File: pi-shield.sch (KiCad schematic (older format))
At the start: 46 parts, among them J1 Conn_02x20_Odd_Even, J10 Conn_01x04, J11 a, J12 Conn_01x03, J2 Conn_01x04, J3 Conn_01x04, J4 0530470210, J5 Conn_01x05, J6 Conn_01x07, J7 0530471410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

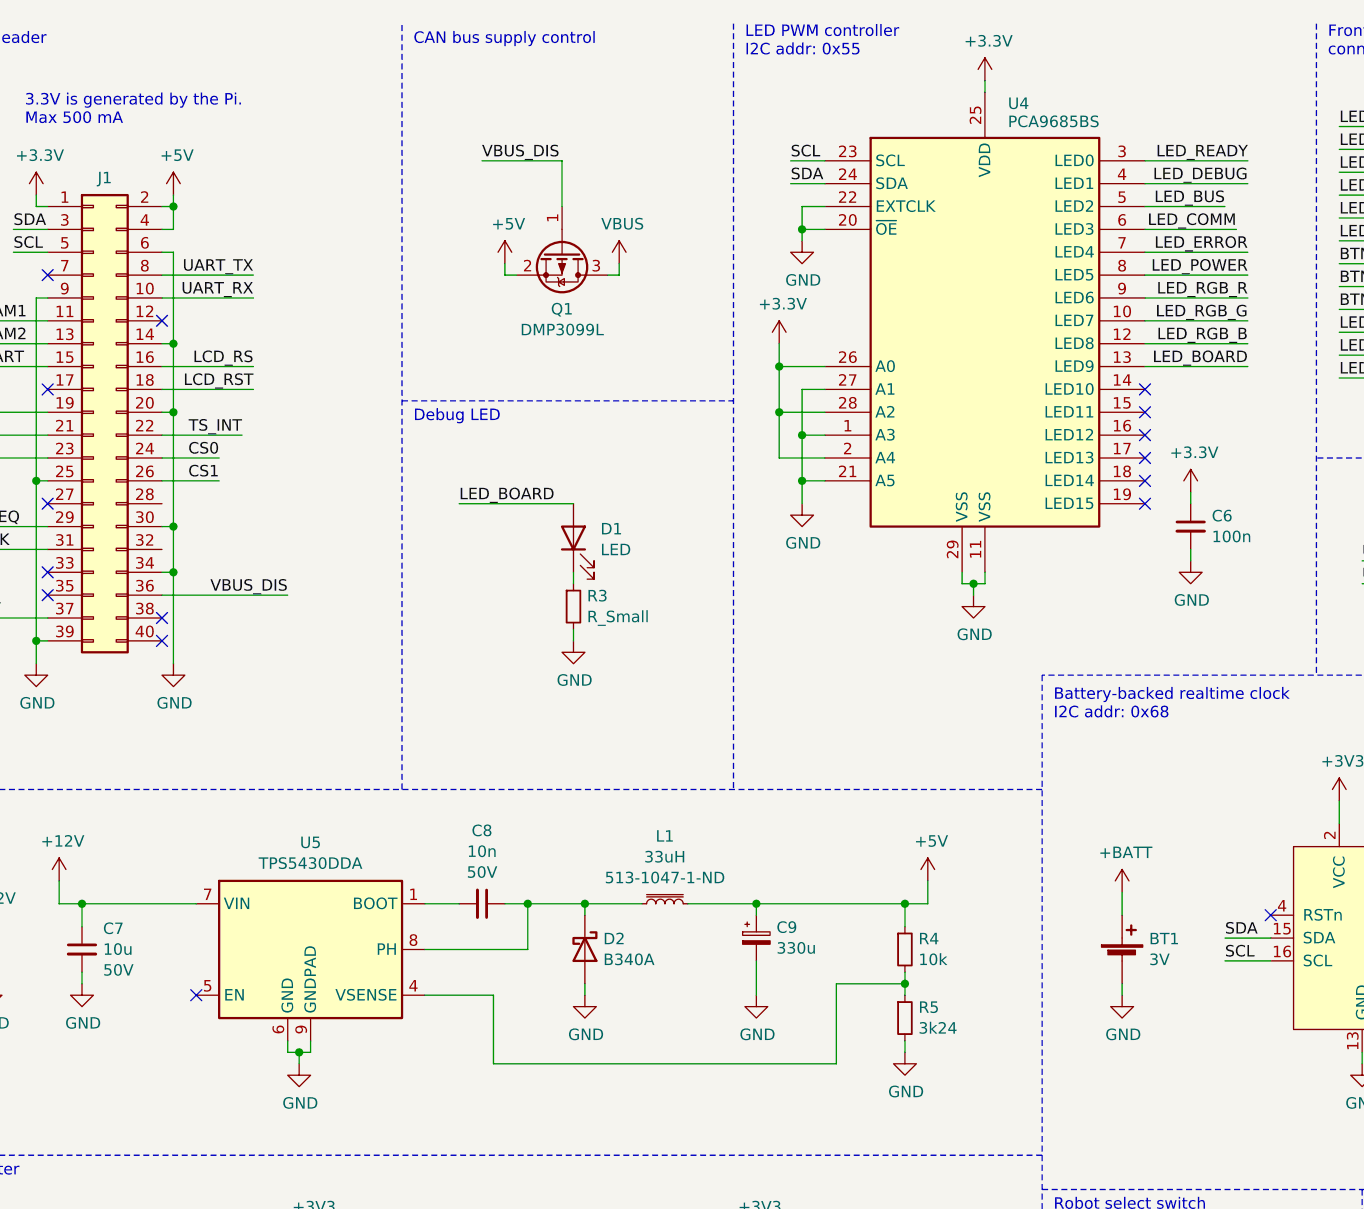
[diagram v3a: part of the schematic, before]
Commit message: Initial component placement
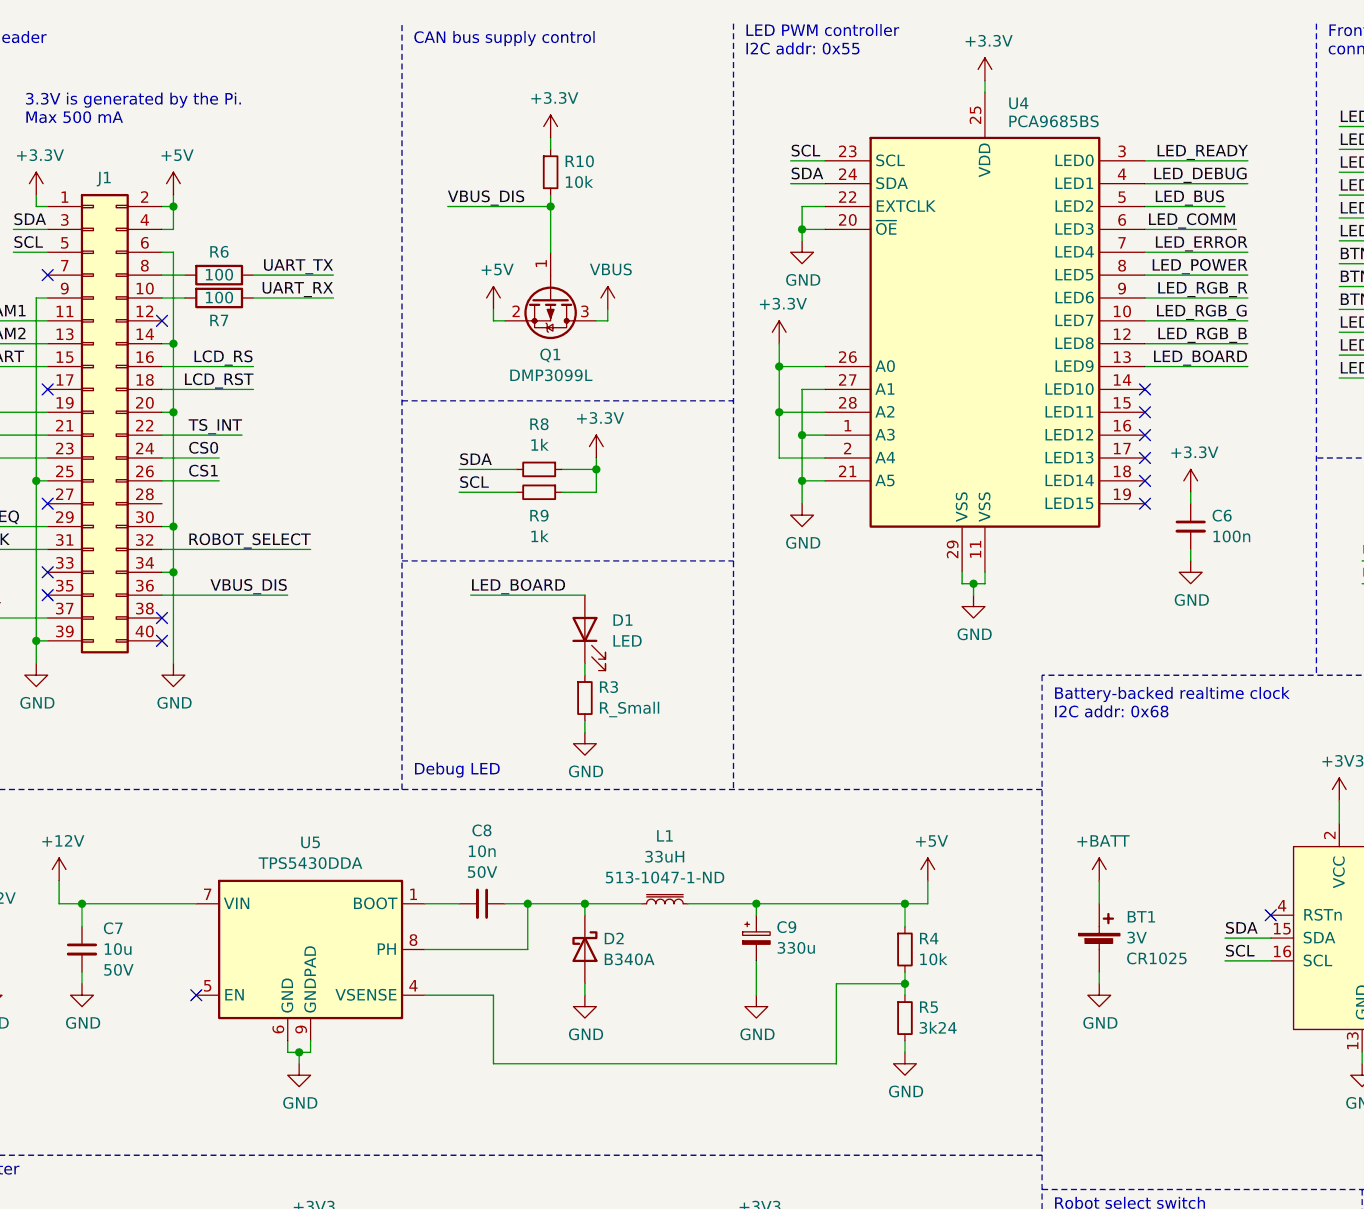
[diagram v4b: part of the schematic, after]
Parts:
- added R10: 10k, Resistor_SMD:R_0603_1608Metric, symbol Device:R_Small
- added R6, R7: 100, Resistor_SMD:R_0603_1608Metric, symbol Device:R
- added R8, R9: 1k, Resistor_SMD:R_0603_1608Metric, symbol Device:R_Small
- BT1: footprint (none) -> pi-shield:3030; battery (none) -> CR1025; digikey# (none) -> 36-3030-ND
- J10: footprint Connector_Molex:Molex_PicoBlade_53048-0410_1x04_P1.25mm_Horizontal -> Connector_Molex:Molex_PicoBlade_53261-0471_1x04-1MP_P1.25mm_Horizontal
- J11: value a -> 0530470210; footprint (none) -> Connector_Molex:Molex_PicoBlade_53398-0271_1x02-1MP_P1.25mm_Vertical
- J2, J3: footprint Connector_Molex:Molex_PicoBlade_53047-0410_1x04_P1.25mm_Vertical -> Connector_Molex:Molex_PicoBlade_53398-0471_1x04-1MP_P1.25mm_Vertical
- L1: footprint (none) -> pi-shield:DR127
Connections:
- net +3V3: now also R10.1, R8.1, R9.1
- net ROBOT_SELECT: now also J1.32 (Pin_32)
- net SCL: now also R9.2
- net SDA: now also R8.2
- net UART_RX: now also R7.1; no longer J1.10 (Pin_10)
- net UART_TX: now also R6.1; no longer J1.8 (Pin_8)
- net VBUS_DIS: now also R10.2
- new net: J1.10 (Pin_10), R7.2
- new net: J1.8 (Pin_8), R6.2
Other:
- moved on the sheet: BT1, D1, Q1, R3

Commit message: Made some progress with layout
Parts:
- R1, R2, R3: footprint Resistor_SMD:R_0805_2012Metric_Pad1.15x1.40mm_HandSolder -> Resistor_SMD:R_0603_1608Metric
- R4, R5: footprint Resistor_SMD:R_0805_2012Metric -> Resistor_SMD:R_0603_1608Metric
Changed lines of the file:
@@
 F 0 "R1" V 3004 7300 50  0000 C CNN
 F 1 "10k" V 3095 7300 50  0000 C CNN
-F 2 "Resistor_SMD:R_0805_2012Metric_Pad1.15x1.40mm_HandSolder" H 3200 7300 50  0001 C CNN
+F 2 "Resistor_SMD:R_0603_1608Metric" H 3200 7300 50  0001 C CNN
 F 3 "~" H 3200 7300 50  0001 C CNN
 	1    3200 7300
@@
 F 0 "R2" H 6591 6346 50  0000 R CNN
 F 1 "10k" H 6591 6255 50  0000 R CNN
-F 2 "Resistor_SMD:R_0805_2012Metric_Pad1.15x1.40mm_HandSolder" H 6650 6300 50  0001 C CNN
+F 2 "Resistor_SMD:R_0603_1608Metric" H 6650 6300 50  0001 C CNN
 F 3 "~" H 6650 6300 50  0001 C CNN
 	1    6650 6300
@@
 F 0 "R3" H 3659 3496 50  0000 L CNN
 F 1 "R_Small" H 3659 3405 50  0000 L CNN
-F 2 "Resistor_SMD:R_0805_2012Metric_Pad1.15x1.40mm_HandSolder" H 3600 3450 50  0001 C CNN
+F 2 "Resistor_SMD:R_0603_1608Metric" H 3600 3450 50  0001 C CNN
 F 3 "~" H 3600 3450 50  0001 C CNN
 	1    3600 3450
@@
 F 0 "R5" H 5059 4896 50  0000 L CNN
 F 1 "3k24" H 5059 4805 50  0000 L CNN
-F 2 "Resistor_SMD:R_0805_2012Metric" H 5000 4850 50  0001 C CNN
+F 2 "Resistor_SMD:R_0603_1608Metric" H 5000 4850 50  0001 C CNN
 F 3 "~" H 5000 4850 50  0001 C CNN
 	1    5000 4850
@@
 F 0 "R4" H 5059 4596 50  0000 L CNN
 F 1 "10k" H 5059 4505 50  0000 L CNN
-F 2 "Resistor_SMD:R_0805_2012Metric" H 5000 4550 50  0001 C CNN
+F 2 "Resistor_SMD:R_0603_1608Metric" H 5000 4550 50  0001 C CNN
 F 3 "~" H 5000 4550 50  0001 C CNN
 	1    5000 4550

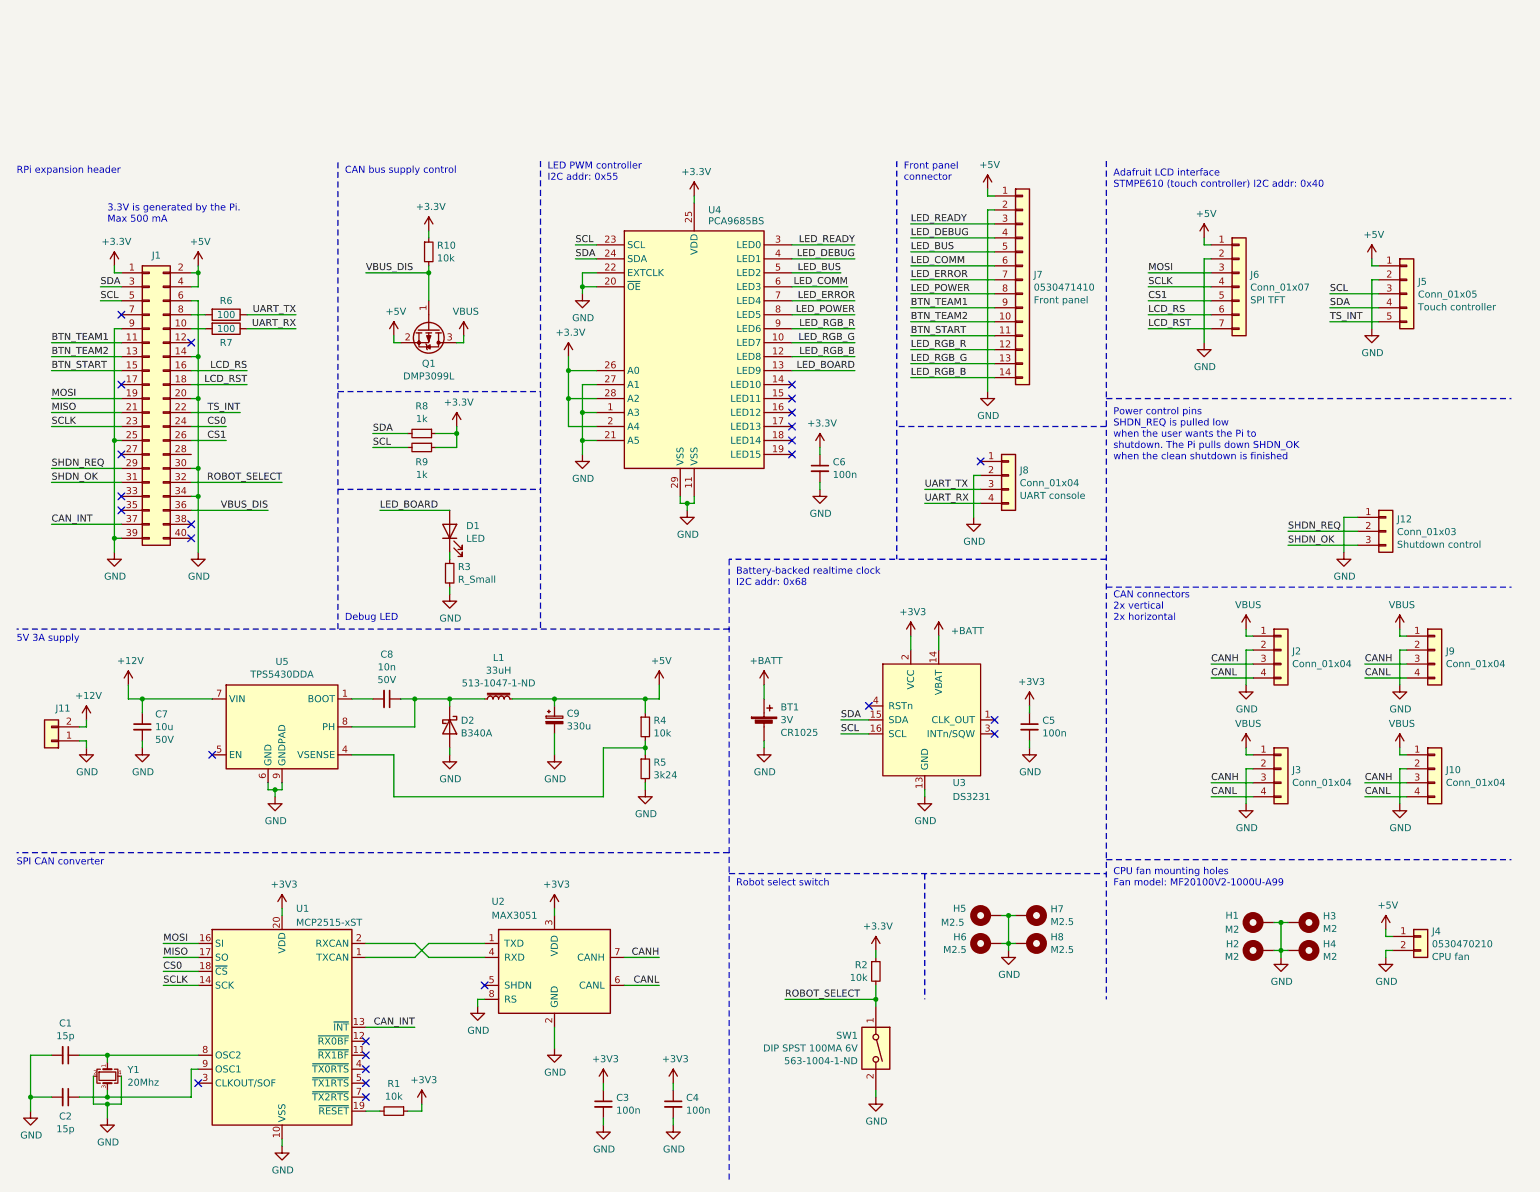
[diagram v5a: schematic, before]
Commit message: First complete layout
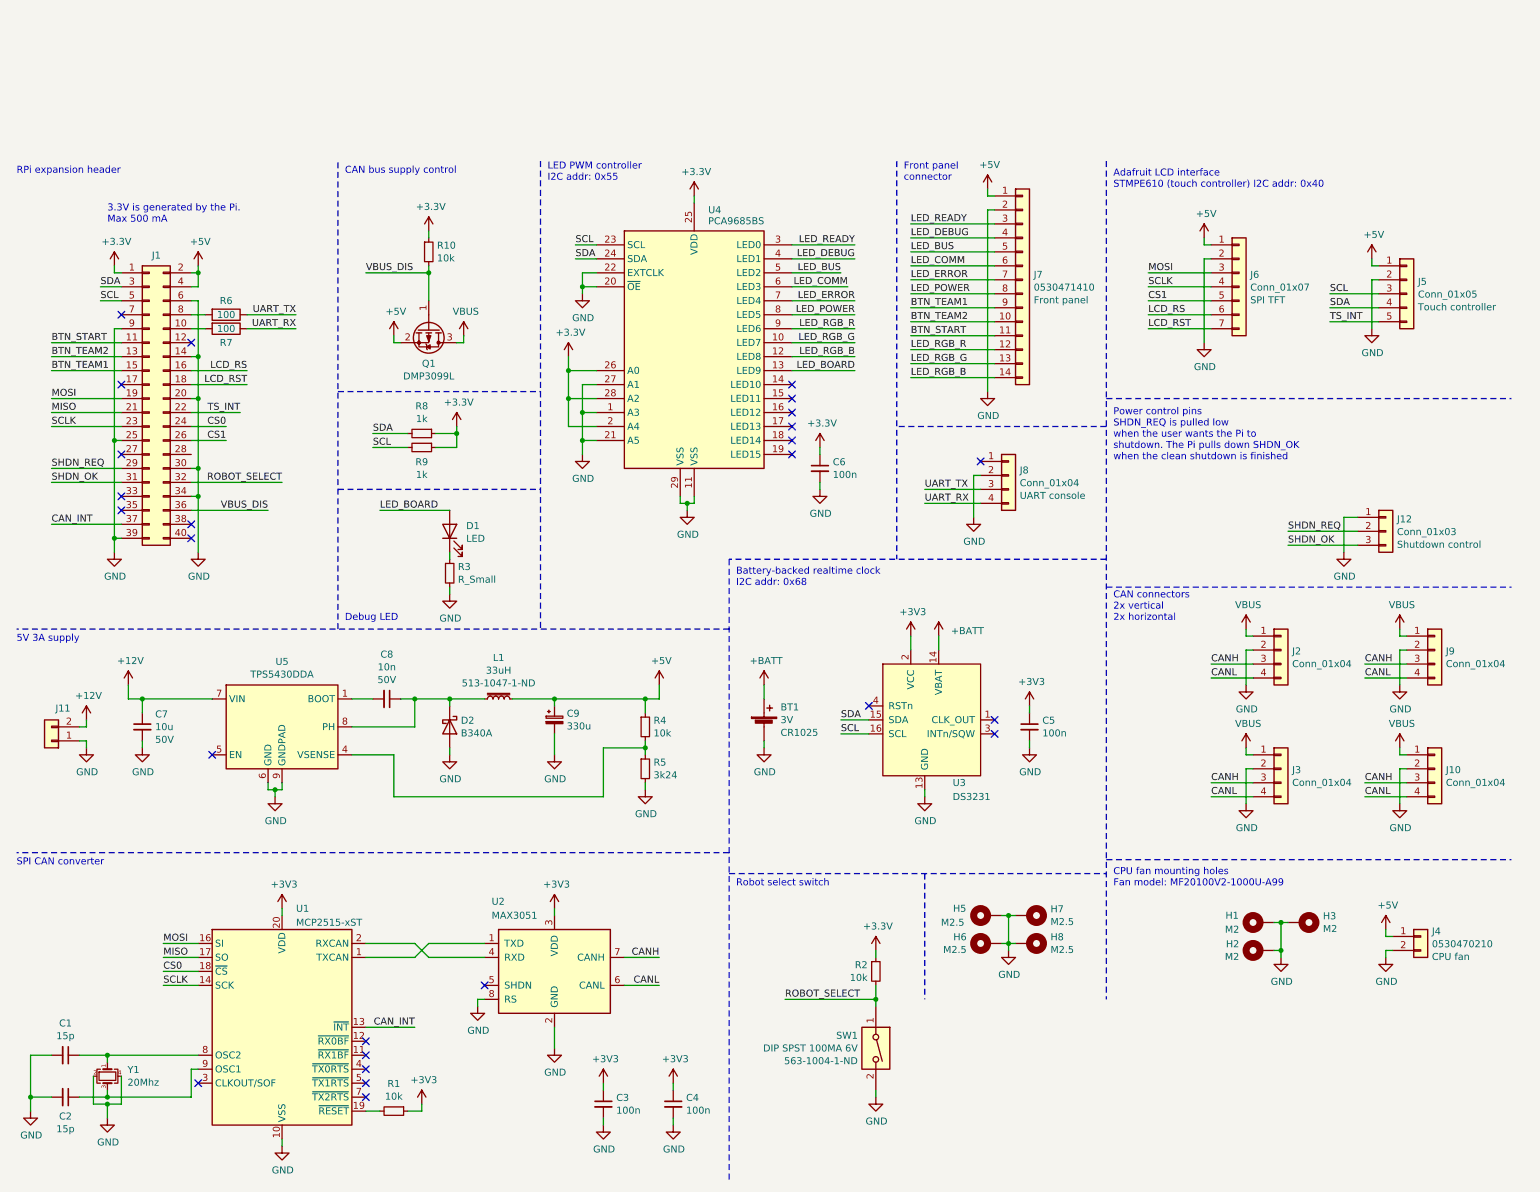
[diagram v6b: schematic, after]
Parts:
- removed H4: M2, MountingHole:MountingHole_2.5mm_Pad_Via, symbol Mechanical:MountingHole_Pad
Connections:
- net BTN_START: now also J1.11 (Pin_11); no longer J1.15 (Pin_15)
- net BTN_TEAM1: now also J1.15 (Pin_15); no longer J1.11 (Pin_11)
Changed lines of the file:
@@
-$EndComp
-$Comp
-L Mechanical:MountingHole_Pad H4
-U 1 1 5F2B9E8F
-P 9700 6150
-F 0 "H4" V 9654 6300 50  0000 L CNN
-F 1 "M2" V 9745 6300 50  0000 L CNN
-F 2 "MountingHole:MountingHole_2.5mm_Pad_Via" H 9700 6150 50  0001 C CNN
-F 3 "~" H 9700 6150 50  0001 C CNN
-	1    9700 6150
-	0    1    1    0
 $EndComp
 $Comp
@@
 NoConn ~ 1750 3100
 NoConn ~ 1750 3200
-Text Label 750  1800 0    50   ~ 0
-BTN_TEAM1
-Text Label 750  1900 0    50   ~ 0
-BTN_TEAM2
-Text Label 750  2000 0    50   ~ 0
-BTN_START
 Wire Wire Line
 	750  2000 1250 2000
@@
 	9550 6200 9550 6150
 Connection ~ 9550 6150
-Wire Wire Line
-	9550 6150 9600 6150
 Wire Wire Line
 	9500 5950 9550 5950
@@
 Wire Wire Line
 	3450 1000 3450 1050
+Text Label 750  1800 0    50   ~ 0
+BTN_START
+Text Label 750  1900 0    50   ~ 0
+BTN_TEAM2
+Text Label 750  2000 0    50   ~ 0
+BTN_TEAM1
 $EndSCHEMATC

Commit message: Prepare for manufacturing adding all digikey#
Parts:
- C1: digikey# (none) -> 399-17621-1-ND
- C3: digikey# (none) -> 399-1169-1-ND
- D1: value LED -> SML-LXT0805IW-TR; digikey# (none) -> 67-1552-1-ND
- J1: digikey# (none) -> 1568-1462-ND
- J11: digikey# (none) -> WM7606CT-ND
- J12: footprint Connector_Molex:Molex_PicoBlade_53398-0471_1x04-1MP_P1.25mm_Vertical -> Connector_Molex:Molex_PicoBlade_53398-0371_1x03-1MP_P1.25mm_Vertical; digikey# (none) -> WM7607CT-ND
- J2: digikey# (none) -> WM7608CT-ND
- J5: digikey# (none) -> WM1745-ND
- J6: digikey# (none) -> WM1747-ND
- J8: digikey# (none) -> WM7622CT-ND
- Q1: digikey# (none) -> DMP3099L-13DICT-ND
- R10: digikey# (none) -> 311-10.0KHRCT-ND
- R3: value R_Small -> 130; digikey# (none) -> 311-130GRCT-ND
- R5: digikey# (none) -> 311-3.24KHRCT-ND
- R6, R7: value 100 -> 130
- R8, R9: value 1k -> 3k24
- U1: digikey# (none) -> MCP2515T-I/STCT-ND
- U2: digikey# (none) -> MAX3051EKA+TCT-ND
- U3: digikey# (none) -> DS3231M+TRLCT-ND
- U4: digikey# (none) -> 568-5305-1-ND
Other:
- moved on the sheet: J12, J5
